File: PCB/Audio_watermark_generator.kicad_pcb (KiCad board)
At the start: 2 copper layers, 25 parts, among them U1 STM32G431KBTx, U4 PAM8303

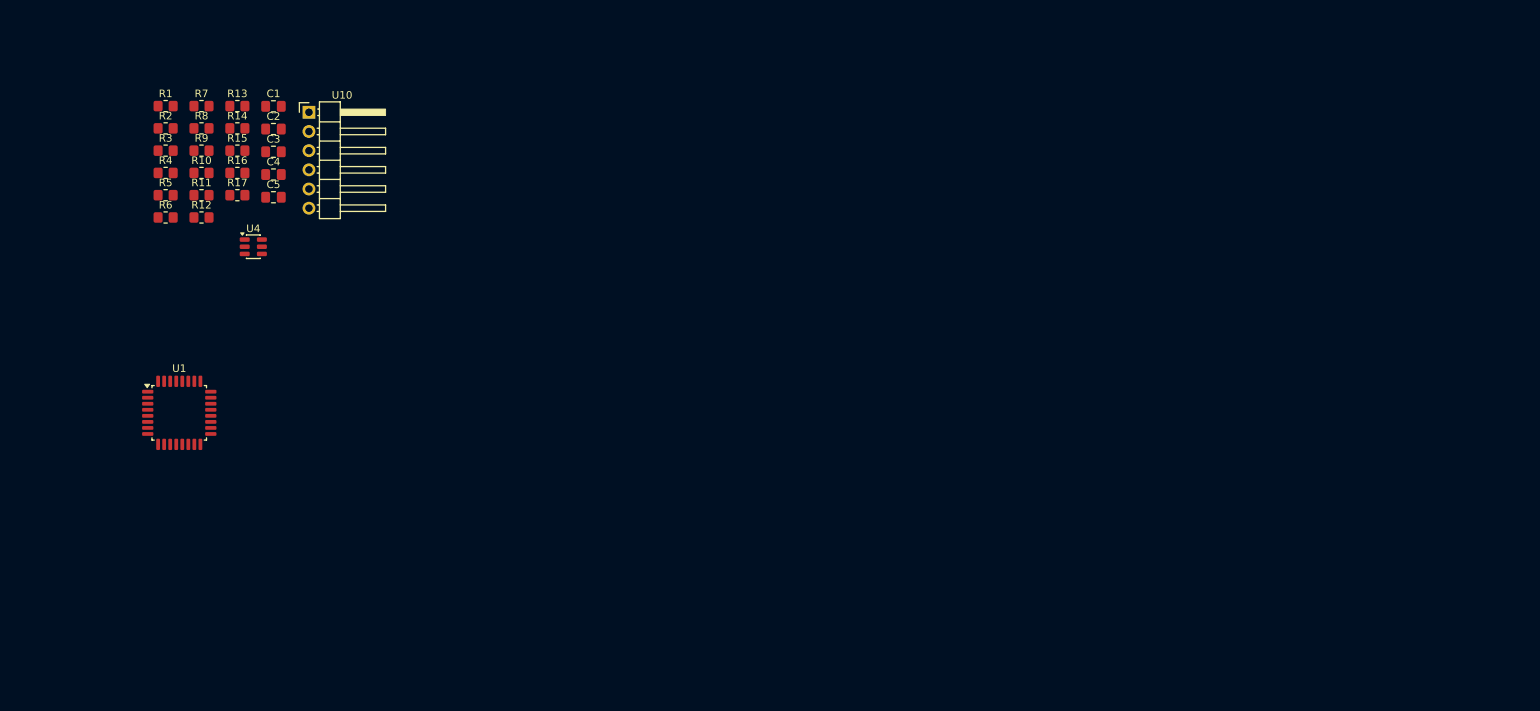
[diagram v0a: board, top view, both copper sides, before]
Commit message: Update component placements and add edge cuts for improved layout in PCB design
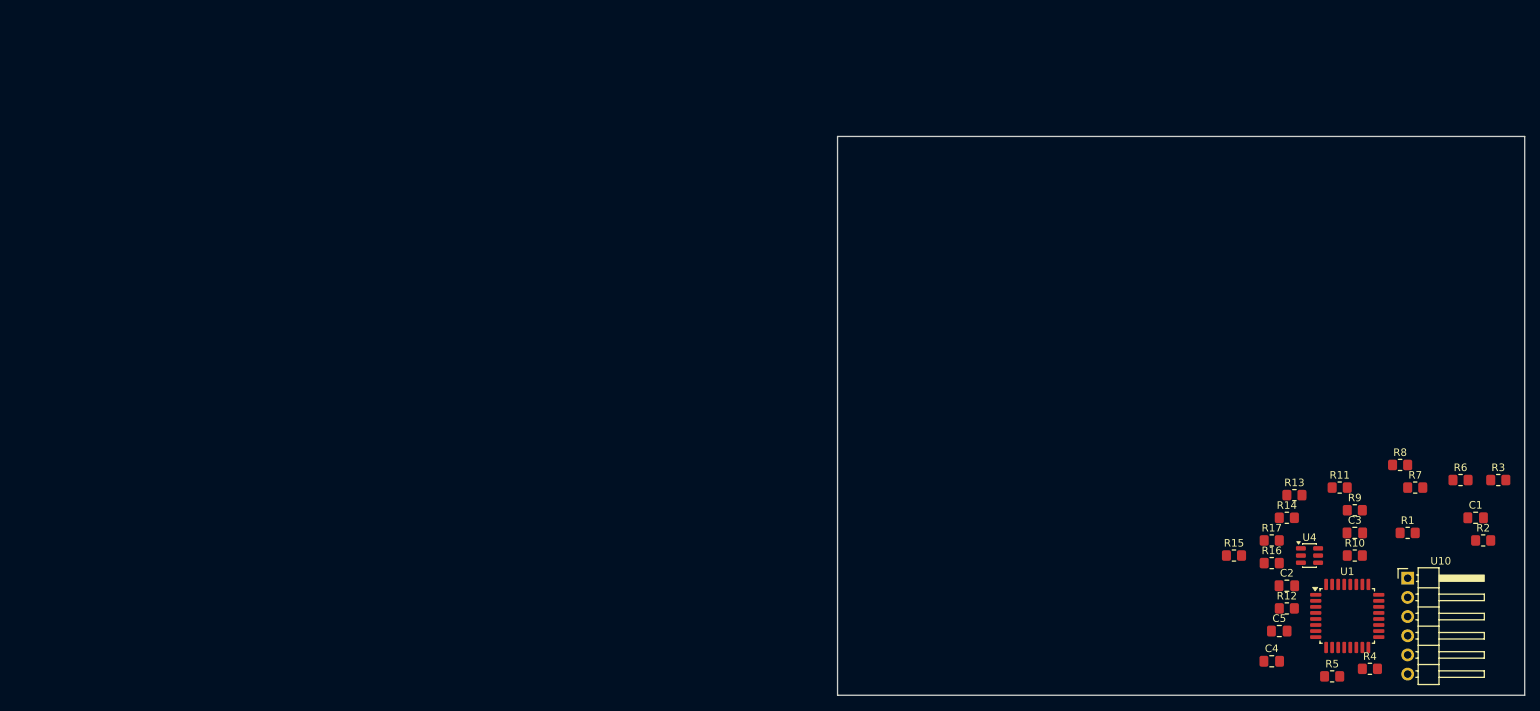
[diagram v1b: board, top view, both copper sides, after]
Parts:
- moved R2 182.8 mm to (219.0, 93.0)
- moved R3 181.8 mm to (221.0, 85.0)
- moved R6 175.0 mm to (216.0, 85.0)
- moved R1 173.9 mm to (209.0, 92.0)
- moved R4 172.5 mm to (204.0, 110.0)
- moved R7 168.5 mm to (210.0, 86.0)
- moved C1 168.3 mm to (218.0, 90.0)
- moved R5 167.1 mm to (199.0, 111.0)
- moved R8 164.9 mm to (208.0, 83.0)
- moved R10 160.9 mm to (202.0, 95.0)
- moved R9 160.0 mm to (202.0, 89.0)
- moved U10 158.0 mm to (209.0, 98.0)
- moved U1 157.0 mm to (201.0, 103.0)
- moved R11 155.6 mm to (200.0, 86.0)
- moved R12 152.8 mm to (193.0, 102.0)
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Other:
- board outline added: 91 x 74 mm

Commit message: Final PCB design with all files included
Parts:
- removed R15, R17: 330R, Resistor_SMD:R_0805_2012Metric_Pad1.20x1.40mm_HandSolder
- removed R16: 1000R, Resistor_SMD:R_0805_2012Metric_Pad1.20x1.40mm_HandSolder
- removed U10: ~, Connector_PinHeader_2.54mm:PinHeader_1x06_P2.54mm_Horizontal
- added B1: 1049_18650_Battery, Battery:1049_KEY_1, B.Cu at (26.1, 64.4)
- added C10: 22uF, Capacitor_SMD:C_0805_2012Metric, F.Cu at (68.0, 33.3)
- added C101: 15pF, Capacitor_SMD:C_0402_1005Metric, F.Cu at (40.8, 29.0)
- added C11: 22uF, Capacitor_SMD:C_0805_2012Metric, F.Cu at (73.8, 28.4)
- added C12: 10uF, Capacitor_SMD:C_0805_2012Metric, F.Cu at (93.0, 40.8)
- added C121: 3p9F, Capacitor_SMD:C_0402_1005Metric, F.Cu at (37.3, 33.8)
- added C122: 8p2F, Capacitor_SMD:C_0402_1005Metric, F.Cu at (34.8, 36.0)
- added C123: 5p6F, Capacitor_SMD:C_0402_1005Metric, F.Cu at (32.8, 34.0)
- added C124: 220pF, Capacitor_SMD:C_0402_1005Metric, F.Cu at (37.3, 32.8)
- added C125: 220pF, Capacitor_SMD:C_0402_1005Metric, F.Cu at (31.3, 34.5)
- added C13: 4n7F, Capacitor_SMD:C_0603_1608Metric, F.Cu at (50.0, 57.0)
- added C131: 3p9F, Capacitor_SMD:C_0402_1005Metric, F.Cu at (38.8, 35.5)
- added C14: 4n7F, Capacitor_SMD:C_0603_1608Metric, F.Cu at (45.6, 63.2)
- added C15: 1uF, Capacitor_SMD:C_0603_1608Metric, F.Cu at (39.4, 61.4)
- added C16: 10uF, Capacitor_SMD:C_0805_2012Metric, F.Cu at (39.1, 59.6)
- added C17: 220pF, Capacitor_SMD:C_0402_1005Metric, F.Cu at (42.8, 56.2)
- added C18: 220pF, Capacitor_SMD:C_0402_1005Metric, F.Cu at (45.5, 56.2)
- added C19: 1uF, Capacitor_SMD:C_0805_2012Metric, F.Cu at (47.4, 28.4)
- added C20: 100nF, Capacitor_SMD:C_0402_1005Metric, F.Cu at (45.8, 34.0)
- added C21: 10nF, Capacitor_SMD:C_0402_1005Metric, F.Cu at (41.8, 30.8)
- added C22: 10nF, Capacitor_SMD:C_0402_1005Metric, F.Cu at (39.0, 37.6)
- added C23: 220pF, Capacitor_SMD:C_0402_1005Metric, F.Cu at (42.8, 38.3)
- added C24: 220pF, Capacitor_SMD:C_0402_1005Metric, F.Cu at (40.0, 37.6)
- added C25: 220pF, Capacitor_SMD:C_0402_1005Metric, F.Cu at (39.0, 31.8)
- added C26: 22uF, Capacitor_SMD:C_0603_1608Metric, F.Cu at (86.2, 30.2)
- added C27: 22uF, Capacitor_SMD:C_0603_1608Metric, F.Cu at (86.2, 33.4)
- added C28: 22uF, Capacitor_SMD:C_0603_1608Metric, F.Cu at (90.6, 35.4)
- added C51: 100nF, Capacitor_SMD:C_0402_1005Metric, F.Cu at (45.8, 33.0)
- added C6: 1uF, Capacitor_SMD:C_0603_1608Metric, F.Cu at (72.2, 37.8)
- added C7: 10pF, Capacitor_SMD:C_0402_1005Metric, F.Cu at (62.2, 55.5)
- added C8: 10pF, Capacitor_SMD:C_0402_1005Metric, F.Cu at (66.2, 53.2)
- added C81: 12pF, Capacitor_SMD:C_0402_1005Metric, F.Cu at (44.1, 29.0)
- added C9: 100nF, Capacitor_SMD:C_0402_1005Metric, F.Cu at (67.8, 52.2)
- added D1: RED, LED_SMD:LED_0603_1608Metric, F.Cu at (59.6, 31.9)
- added FB1: 120R, Inductor_SMD:L_0603_1608Metric, F.Cu at (74.9, 38.8)
- added FB2: 600R, Inductor_SMD:L_0603_1608Metric, F.Cu at (42.5, 57.8)
- added FB3: 600R, Inductor_SMD:L_0603_1608Metric, F.Cu at (45.7, 57.8)
- added FB4: 1kR, Inductor_SMD:L_0402_1005Metric, F.Cu at (46.9, 26.8)
- added IC1: STM32G431KBT6, STM32G431KBT6:STM32G431KBT6, F.Cu at (64.6, 44.1)
- added IC2: ISL91107IRTNZ-T7A, Battery:QFN50P300X400X80-21N, F.Cu at (89.9, 31.9)
- added J1: USB_B_Micro, Connector_USB:USB_Micro-B_Wuerth_629105150521, F.Cu at (63.8, 27.3)
- added J2: Conn_01x03, Connector_PinHeader_2.54mm:PinHeader_1x03_P2.54mm_Vertical_SMD_Pin1Right, F.Cu at (33.1, 59.9)
- added J3: Conn_01x04_Pin, Connector_PinHeader_2.54mm:PinHeader_1x04_P2.54mm_Vertical, F.Cu at (106.7, 51.0)
- added J4: SJ2-35954A-SMT-TR, Connector_Audio:CUI_SJ2-35954A-SMT-TR, F.Cu at (72.9, 59.0)
- added J5: SJ2-35954A-SMT-TR, Connector_Audio:CUI_SJ2-35954A-SMT-TR, F.Cu at (55.7, 59.0)
- added J6: 533980271_Picoblade, Connector:MOLEX_533980271_Picoblade, F.Cu at (44.1, 52.0)
- added J7: CONSMA002-SMD-G-T, Connector:LINX_CONSMA002-SMD-G-T, F.Cu at (30.8, 44.5)
- added J8: Conn_01x01_Pin, TestPoint:TestPoint_Pad_2.0x2.0mm, F.Cu at (28.6, 28.4)
- added K1: AGQ210S03, Relay_SMD:AGQ210S03, F.Cu at (84.1, 59.3)
- added L1: 1uH, Inductor_SMD:L_1008_2520Metric, F.Cu at (94.4, 31.8)
- added L121: 27nH, Inductor_SMD:L_0402_1005Metric, F.Cu at (38.8, 33.3)
- added L122: 22nH, Inductor_SMD:L_0402_1005Metric, F.Cu at (35.3, 34.4)
- added L123: 27nH, Inductor_SMD:L_0402_1005Metric, F.Cu at (33.2, 35.5)
- added L131: 27nH, Inductor_SMD:L_0402_1005Metric, F.Cu at (37.3, 35.0)
- added R171: 56kR, Resistor_SMD:R_0402_1005Metric, F.Cu at (41.8, 38.3)
- added SW1: SW_SPDT, Button_Switch_SMD:SW_SPDT_PCM12, F.Cu at (53.7, 26.7)
- added SW2: SW_SPDT, Button_Switch_SMD:SW_SPDT_PCM12, F.Cu at (90.7, 26.7)
- added U2: L9110S, Driver:SOIC127P599X172-8N, F.Cu at (93.6, 53.6)
- added U3: MCP6072, OpAmp:SOIC127P599X175-8N, F.Cu at (86.1, 46.2)
- added U5: PAM8304, Audio_Module:PAM8304ASR, F.Cu at (44.1, 60.4)
- added U7: RTC_DS3231, Connector_PinHeader_2.54mm:PinHeader_1x06_P2.54mm_DS3231, F.Cu at (106.6, 31.1)
- added U8: CC1101, RF_Module:CC1101, F.Cu at (42.4, 34.6)
- added Y1: 16MHz, Crystal:Crystal_SMD_3225-4Pin_3.2x2.5mm, F.Cu at (63.6, 53.1)
- added Y2: NX3225GA-26MHZ-EXS00A-CG01972, Crystal:Crystal_SMD_3225-4Pin_3.2x2.5mm, F.Cu at (42.9, 26.6)
- C1: value 1000nF -> 4u7F; footprint Capacitor_SMD:C_0805_2012Metric_Pad1.18x1.45mm_HandSolder -> Capacitor_SMD:C_0603_1608Metric
- C2, C3: value 3.3nF -> 100nF; footprint Capacitor_SMD:C_0805_2012Metric_Pad1.18x1.45mm_HandSolder -> Capacitor_SMD:C_0402_1005Metric
- C4: value 1000nF -> 10nF; footprint Capacitor_SMD:C_0805_2012Metric_Pad1.18x1.45mm_HandSolder -> Capacitor_SMD:C_0402_1005Metric
- C5: value 1000nF -> 1uF; footprint Capacitor_SMD:C_0805_2012Metric_Pad1.18x1.45mm_HandSolder -> Capacitor_SMD:C_0603_1608Metric
- R1: value 3300R -> 1k5R; footprint Resistor_SMD:R_0805_2012Metric_Pad1.20x1.40mm_HandSolder -> Resistor_SMD:R_0402_1005Metric
- R10: value 500000R -> 1kR; footprint Resistor_SMD:R_0805_2012Metric_Pad1.20x1.40mm_HandSolder -> Resistor_SMD:R_0805_2012Metric
- R11: value 10000R -> 1MR; footprint Resistor_SMD:R_0805_2012Metric_Pad1.20x1.40mm_HandSolder -> Resistor_SMD:R_0805_2012Metric
- R12: value 10000R -> 1kR; footprint Resistor_SMD:R_0805_2012Metric_Pad1.20x1.40mm_HandSolder -> Resistor_SMD:R_0805_2012Metric
- R13: value 1000R -> 330kR; footprint Resistor_SMD:R_0805_2012Metric_Pad1.20x1.40mm_HandSolder -> Resistor_SMD:R_0805_2012Metric
- R14: value 330R -> 330kR; footprint Resistor_SMD:R_0805_2012Metric_Pad1.20x1.40mm_HandSolder -> Resistor_SMD:R_0805_2012Metric
- R2: value 10000R -> 10kR; footprint Resistor_SMD:R_0805_2012Metric_Pad1.20x1.40mm_HandSolder -> Resistor_SMD:R_0402_1005Metric
- R3: value 10000R -> 100kR; footprint Resistor_SMD:R_0805_2012Metric_Pad1.20x1.40mm_HandSolder -> Resistor_SMD:R_0805_2012Metric
- R4, R5: value 100000R -> 100kR; footprint Resistor_SMD:R_0805_2012Metric_Pad1.20x1.40mm_HandSolder -> Resistor_SMD:R_0805_2012Metric
- R6: value 1000R -> 100kR; footprint Resistor_SMD:R_0805_2012Metric_Pad1.20x1.40mm_HandSolder -> Resistor_SMD:R_0805_2012Metric
- R7: value 1000000R -> 2kR; footprint Resistor_SMD:R_0805_2012Metric_Pad1.20x1.40mm_HandSolder -> Resistor_SMD:R_0805_2012Metric
- R8: value 1000R -> 10kR; footprint Resistor_SMD:R_0805_2012Metric_Pad1.20x1.40mm_HandSolder -> Resistor_SMD:R_0805_2012Metric
- R9: value 10000000R -> 10kR; footprint Resistor_SMD:R_0805_2012Metric_Pad1.20x1.40mm_HandSolder -> Resistor_SMD:R_0805_2012Metric
- U1: value STM32G431KBTx -> AMS1117-3.3; footprint Package_QFP:LQFP-32_7x7mm_P0.8mm -> Package_TO_SOT_SMD:SOT-223-3_TabPin2
- U4: value PAM8303 -> MCP6072; footprint Package_TO_SOT_SMD:SOT-23-6 -> OpAmp:SOIC127P599X175-8N
- moved R2 177.6 mm to (52.9, 30.1), turned to -90 degrees
- moved R1 163.4 mm to (57.3, 31.4), turned to 90 degrees
- moved C1 162.8 mm to (59.8, 51.7), turned to 180 degrees
- moved R14 153.1 mm to (42.2, 63.2)
- moved R3 149.8 mm to (81.6, 30.2), turned to 90 degrees
- moved R13 146.4 mm to (50.0, 60.4), turned to 90 degrees
- moved U1 145.2 mm to (73.5, 33.4)
- moved C3 144.5 mm to (67.9, 38.4)
- moved R4 144.3 mm to (81.6, 33.6), turned to 90 degrees
- moved C2 140.8 mm to (60.9, 50.3), turned to 180 degrees
- moved C4 137.9 mm to (70.7, 41.7), turned to 90 degrees
- moved C5 136.3 mm to (72.2, 39.8), turned to 180 degrees
- moved R6 135.4 mm to (84.6, 52.2), turned to -90 degrees
- moved R10 131.9 mm to (82.0, 40.2)
- moved R11 130.9 mm to (76.1, 43.8), turned to 90 degrees
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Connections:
- C1 pad 1: Net-(C1-Pad1) -> +3.3V
- C1 pad 2: Net-(C1-Pad2) -> GND
- C2 pad 1: GND -> +3.3V
- C2 pad 2: Net-(C2-Pad2) -> GND
- C3 pad 1: Net-(C3-Pad1) -> +3.3V
- C3 pad 2: Net-(C3-Pad2) -> GND
- C4 pad 1: GND -> +3.3VA
- C4 pad 2: +3.3V -> GND
- C5 pad 1: +3.3V -> +3.3VA
- R1 pad 1: +3.3V -> Net-(D1-K)
- R1 pad 2: Net-(C1-Pad1) -> GND
- R10 pad 1: Net-(C3-Pad1) -> Net-(U4B--)
- R11 pad 1: Net-(U4-IN) -> Net-(U4B--)
- R11 pad 2: Net-(C3-Pad2) -> Net-(U4A--)
- R12 pad 1: Net-(U4-IN-) -> Net-(K1-Pad2)
- R12 pad 2: Net-(C2-Pad2) -> Net-(U4B--)
- R13 pad 1: GND -> Net-(U5-IN+)
- R13 pad 2: Net-(U8A-+) -> Net-(C13-Pad2)
- R14 pad 2: Net-(U8A-+) -> Net-(C14-Pad2)
- R2 pad 1: Net-(U2A--) -> /STM32/SW_BOOT0
- R2 pad 2: Net-(C1-Pad2) -> /STM32/BOOT0
- R3 pad 1: Net-(R3-Pad1) -> /STM32/BAT_ADC
- R3 pad 2: Net-(U2A--) -> /Battery/V_BAT
- R4 pad 1: +3.3V -> GND
- R4 pad 2: Net-(U7A-+) -> /STM32/BAT_ADC
- R5 pad 1: Net-(U7A-+) -> +3.3V
- R5 pad 2: GND -> Net-(U3A-+)
- R6 pad 1: Net-(U6A--) -> Net-(U3A-+)
- R6 pad 2: Net-(R3-Pad1) -> GND
- R7 pad 1: Net-(U6A--) -> +3.3V
- R8 pad 1: Net-(R8-Pad1) -> Net-(U3B--)
- R8 pad 2: Net-(U6A--) -> Net-(C12-Pad2)
- R9 pad 2: Net-(U1-PA4) -> Net-(U3B--)
- U1 pad 1: unconnected-(U1-VDD-Pad1) -> GND
- U1 pad 2: unconnected-(U1-PF0-Pad2) -> +3.3V
- U1 pad 3: unconnected-(U1-PF1-Pad3) -> VBUS
- U4 pad 1: unconnected-(U4-OUT--Pad1) -> Net-(U4A--)
- U4 pad 2: GND -> Net-(U4A--)
- U4 pad 3: Net-(U4-IN) -> /Mixer/DAC
- U4 pad 4: Net-(U4-IN-) -> GND
- U4 pad 5: +3.3V -> Net-(U3A--)
- U4 pad 6: Net-(U1-PA7) -> Net-(U4B--)
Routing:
- net GND: track 0.00 -> 122.1 mm, vias 0 -> 86
- net /STM32/SWCLK: track 0.00 -> 62.5 mm, vias 0 -> 2
- net /STM32/SWDIO: track 0.00 -> 58.5 mm, vias 0 -> 2
- net +3.3V: track 0.00 -> 55.2 mm, vias 0 -> 16
- net /STM32/PA2: track 0.00 -> 50.6 mm, vias 0 -> 2
- net /Transceiver/VCC_CC1101: track 0.00 -> 49.4 mm, vias 0 -> 5
- net /STM32/PA3: track 0.00 -> 46.2 mm, vias 0 -> 2
- net /Mixer/DAC: track 0.00 -> 44.9 mm, vias 0 -> 4
- net /RTC/SDA: track 0.00 -> 43.5 mm
- net /RTC/SCL: track 0.00 -> 43.4 mm
- net /RTC/RTC_PWR: track 0.00 -> 41.3 mm
- net /STM32/SPEAKER_EN: track 0.00 -> 39.7 mm, vias 0 -> 2
- net Net-(C12-Pad1): track 0.00 -> 39.6 mm
- net Net-(SW2-C): track 0.00 -> 39.4 mm
- net /STM32/PA15: track 0.00 -> 36.4 mm, vias 0 -> 2
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- added copper zone on In2.Cu, net +3.3V
- added copper zone on In1.Cu, net GND
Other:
- board size 91 x 74 mm -> 83 x 41 mm
- copper layers 2 -> 4
- board text added: "BOOT"
- board text added: "EB-KG"
- board text added: "IN"
- board text added: "OFF"
- board text added: "ON"
- board text added: "OUT"
- board text added: "PA15"
- board text added: "PA2"
- board text added: "PA3"
- board text added: "SCL"
- board text added: "SDA"
- board text added: "SWCLK"
- board text added: "SWDIO"
- board text added: "USB"

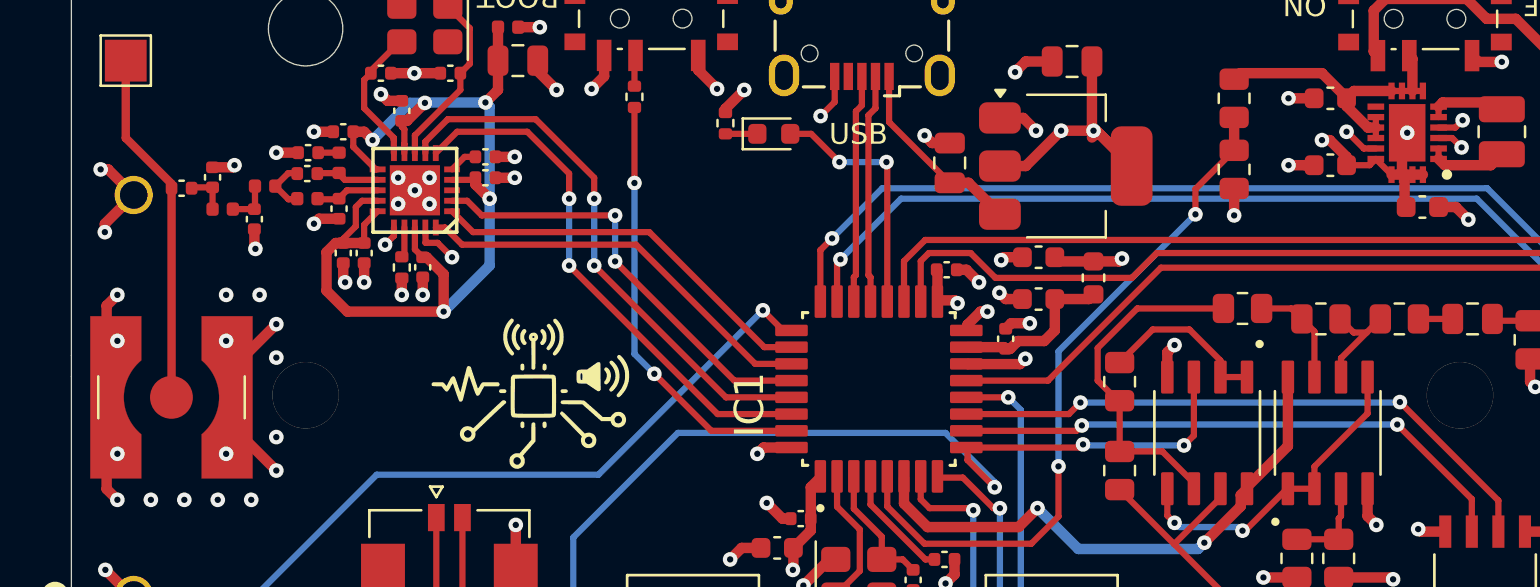
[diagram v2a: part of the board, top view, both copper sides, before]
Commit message: Update PCB settings and add new VIP net class
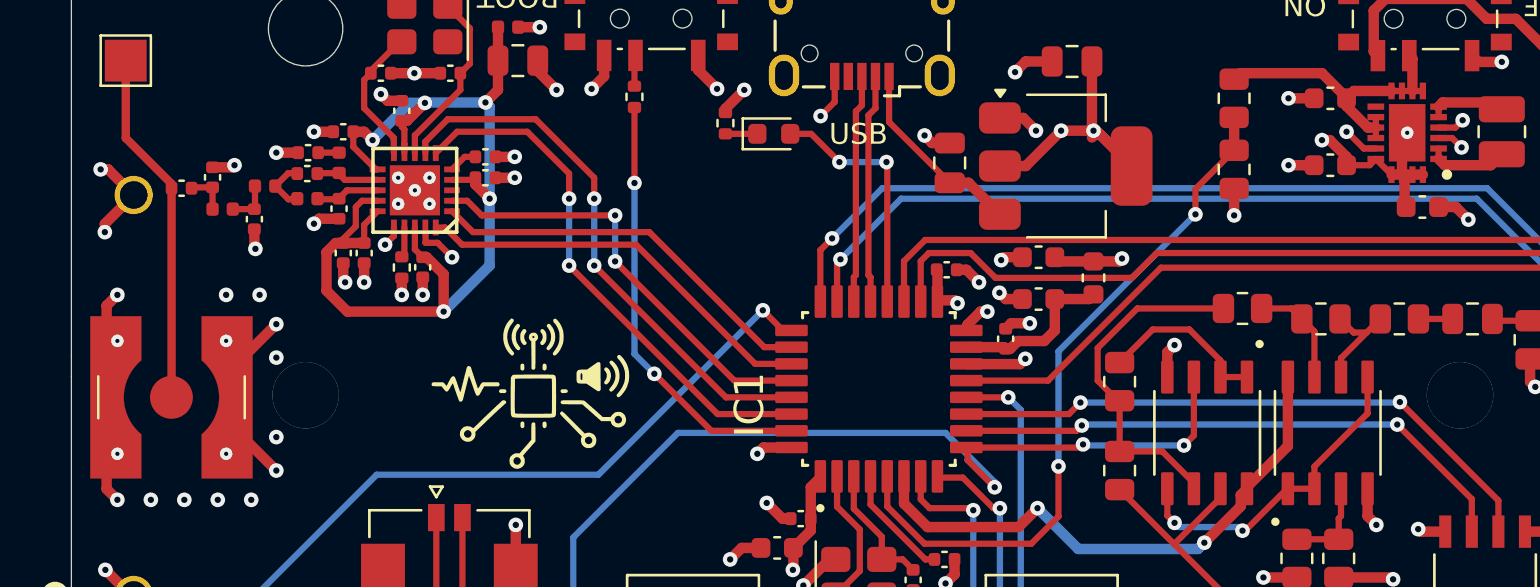
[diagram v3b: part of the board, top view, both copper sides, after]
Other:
- board text added: "VIA IN PAD - EPOXY FILLED & CAPPED"
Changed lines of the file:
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@@
 		(tenting front back)
 		(pcbplotparams
-			(layerselection 0x00000000_00000000_55555555_5755f5ff)
+			(layerselection 0x00000000_00000000_55555555_5775f5ff)
 			(plot_on_all_layers_selection 0x00000000_00000000_00000000_00000000)
 			(disableapertmacros no)
@@
 		(layer "F.SilkS")
 	)
+	(gr_circle
+		(center 33.4 47.2)
+		(end 33.8 47.2)
+		(stroke
+			(width 0.1)
+			(type solid)
+		)
+		(fill no)
+		(layer "Eco1.User")
+	)
+	(gr_circle
+		(center 28.2 47.2)
+		(end 28.6 47.2)
+		(stroke
+			(width 0.1)
+			(type solid)
+		)
+		(fill no)
+		(layer "Eco1.User")
+	)
+	(gr_circle
+		(center 43.125 34)
+		(end 43.525 34)
+		(stroke
+			(width 0.1)
+			(type solid)
+		)
+		(fill no)
+		(layer "Eco1.User")
+	)
+	(gr_circle
+		(center 89.875 31.85)
+		(end 90.275 31.85)
+		(stroke
+			(width 0.1)
+			(type solid)
+		)
+		(fill no)
+		(layer "Eco1.User")
+	)
+	(gr_circle
+		(center 33.4 41.8)
+		(end 33.8 41.8)
+		(stroke
+			(width 0.1)
+			(type solid)
+		)
+		(fill no)
+		(layer "Eco1.User")
+	)
+	(gr_circle
+		(center 28.2 41.8)
+		(end 28.6 41.8)
+		(stroke
+			(width 0.1)
+			(type solid)
+		)
+		(fill no)
+		(layer "Eco1.User")
+	)
+	(gr_circle
+		(center 41.625 34)
+		(end 41.625 33.6)
+		(stroke
+			(width 0.1)
+			(type solid)
+		)
+		(fill no)
+		(layer "Eco1.User")
+	)
+	(gr_circle
+		(center 42.425 34.6)
+		(end 42.825 34.6)
+		(stroke
+			(width 0.1)
+			(type solid)
+		)
+		(fill no)
+		(layer "Eco1.User")
+	)
+	(gr_circle
+		(center 43.125 35.25)
+		(end 43.525 35.25)
+		(stroke
+			(width 0.1)
+			(type solid)
+		)
+		(fill no)
+		(layer "Eco1.User")
+	)
+	(gr_circle
+		(center 41.625 35.25)
+		(end 42.025 35.25)
+		(stroke
+			(width 0.1)
+			(type solid)
+		)
+		(fill no)
+		(layer "Eco1.User")
+	)
 	(gr_poly
 		(pts
@@
 		)
 	)
+	(gr_text "VIA IN PAD - EPOXY FILLED & CAPPED"
+		(at 43.525 37.025 0)
+		(layer "Eco1.User")
+		(effects
+			(font
+				(size 1 1)
+				(thickness 0.15)
+			)
+			(justify left bottom)
+		)
+	)
 	(segment
 		(start 47.0383 60.0875)
@@
 	(via
 		(at 28.2 47.2)
-		(size 0.7)
-		(drill 0.3)
+		(size 0.6)
+		(drill 0.2)
 		(layers "F.Cu" "B.Cu")
 		(net 1)
@@
 	(via
 		(at 42.425 34.6)
-		(size 0.7)
-		(drill 0.3)
+		(size 0.6)
+		(drill 0.2)
 		(layers "F.Cu" "B.Cu")
 		(net 1)
@@
 	(via
 		(at 28.2 41.8)
-		(size 0.7)
-		(drill 0.3)
+		(size 0.6)
+		(drill 0.2)
 		(layers "F.Cu" "B.Cu")
 		(net 1)
@@
 	(via
 		(at 43.125 35.25)
-		(size 0.7)
-		(drill 0.3)
+		(size 0.6)
+		(drill 0.2)
 		(layers "F.Cu" "B.Cu")
 		(net 1)
@@
 	(via
 		(at 41.625 34)
-		(size 0.7)
-		(drill 0.3)
+		(size 0.6)
+		(drill 0.2)
 		(layers "F.Cu" "B.Cu")
 		(net 1)
@@
 	(via
 		(at 33.4 47.2)
-		(size 0.7)
-		(drill 0.3)
+		(size 0.6)
+		(drill 0.2)
 		(layers "F.Cu" "B.Cu")
 		(net 1)
@@
 	(via
 		(at 43.125 34)
-		(size 0.7)
-		(drill 0.3)
+		(size 0.6)
+		(drill 0.2)
 		(layers "F.Cu" "B.Cu")
 		(net 1)
@@
 	(via
 		(at 33.4 41.8)
-		(size 0.7)
-		(drill 0.3)
+		(size 0.6)
+		(drill 0.2)
 		(layers "F.Cu" "B.Cu")
 		(net 1)
@@
 	(via
 		(at 41.625 35.25)
-		(size 0.7)
-		(drill 0.3)
+		(size 0.6)
+		(drill 0.2)
 		(layers "F.Cu" "B.Cu")
 		(net 1)
@@
 	(via
 		(at 89.874998 31.85)
-		(size 0.7)
-		(drill 0.3)
+		(size 0.6)
+		(drill 0.2)
 		(layers "F.Cu" "B.Cu")
 		(net 2)

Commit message: Update Gerber files and creation dates for Audio Watermark Generator project
- Updated creation dates in all Gerber files to reflect the new timestamp of 2026-03-25T20:04:04+01:00.
- Added new Gerber files: Audio_watermark_generator-gm6.gbr and Audio_watermark_generator-gm7.gbr.
- Modified drill files (NPTH and PTH) to update creation dates.
- Updated job file to include new creation date and added references for new Gerber files.
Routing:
- net GND: track 122.1 -> 121.4 mm
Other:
- board text added: "VIA IN PAD - CAPPED"
- board text added: "VIA IN PAD - EPOXY FILLED"
- board text removed: "VIA IN PAD - EPOXY FILLED & CAPPED"
